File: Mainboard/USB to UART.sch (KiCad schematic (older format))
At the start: 8 parts, among them U9 CH340B

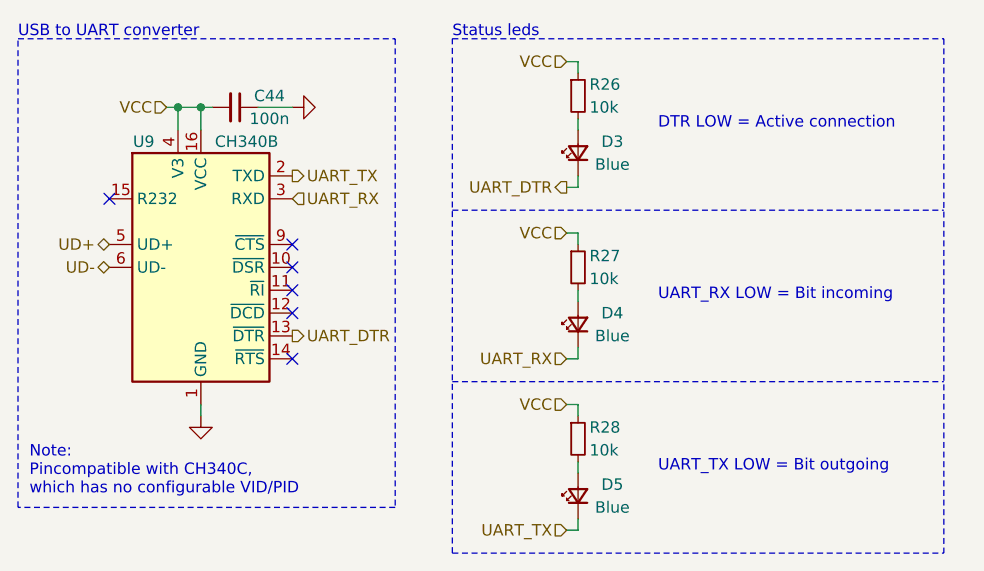
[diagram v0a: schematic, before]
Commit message: Before power tree change
Backup before switching from two to one LDO
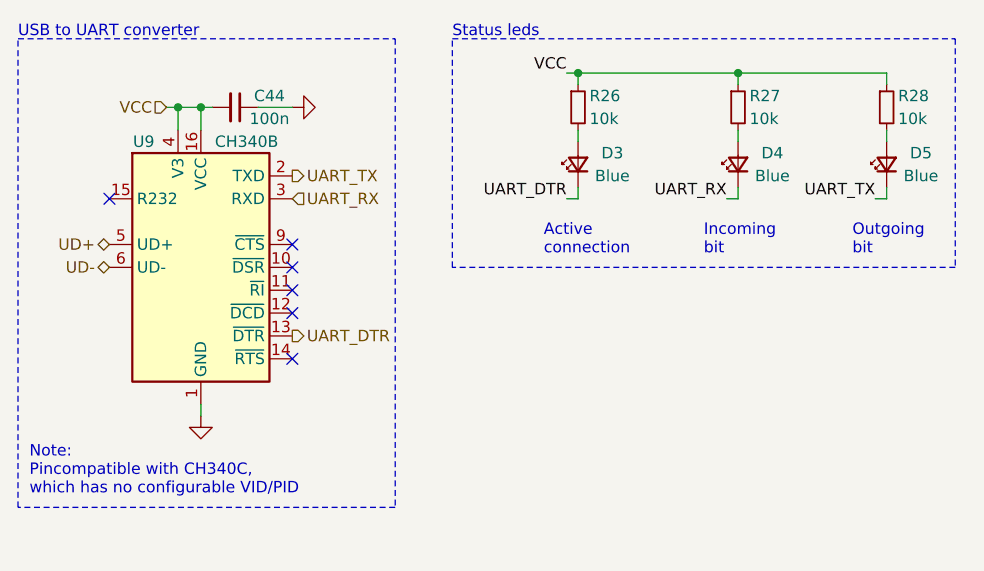
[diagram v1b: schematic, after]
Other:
- note added: "Active\nconnection"
- note added: "Incoming\nbit"
- note added: "Outgoing\nbit"
- note removed: "DTR LOW = Active connection"
- note removed: "UART_RX LOW = Bit incoming"
- note removed: "UART_TX LOW = Bit outgoing"
- moved on the sheet: D3, D4, D5, R26, R27, R28
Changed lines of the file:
@@
 Sheet 2 9
 Title "4x38W amp with DSP and BT"
-Date "2021-06-08"
-Rev "0.1"
+Date "2021-11-08"
+Rev "0.2"
 Comp "ZOUDIO"
 Comment1 ""
@@
 Wire Notes Line
 	5650 2800 5650 4850
-Wire Notes Line
-	5900 5050 8050 5050
-Wire Notes Line
-	5900 4300 8050 4300
-Wire Notes Line
-	5900 3550 8050 3550
 Text Notes 5900 2800 0    50   ~ 0
 Status leds
 Wire Notes Line
-	5900 5050 5900 2800
-Wire Notes Line
-	8050 2800 8050 5050
-Wire Notes Line
-	5900 2800 8050 2800
-Text HLabel 6400 3450 0    50   Output ~ 0
-UART_DTR
-Wire Wire Line
-	6400 4950 6450 4950
-Wire Wire Line
-	6400 4200 6450 4200
-Text HLabel 6400 4950 0    50   Input ~ 0
-UART_TX
-Text HLabel 6400 4200 0    50   Input ~ 0
-UART_RX
-Text Notes 6800 4700 0    50   ~ 0
-UART_TX LOW = Bit outgoing
-Text Notes 6800 3950 0    50   ~ 0
-UART_RX LOW = Bit incoming
-Wire Wire Line
-	6450 3450 6400 3450
-Wire Wire Line
-	6450 3400 6450 3450
-Wire Wire Line
-	6450 2900 6450 2950
-Wire Wire Line
-	6450 3150 6450 3200
+	5900 3800 5900 2800
+Wire Notes Line
+	5900 2800 8100 2800
+Wire Wire Line
+	7750 3500 7800 3500
+Wire Wire Line
+	7100 3500 7150 3500
+Wire Wire Line
+	6450 3500 6400 3500
+Wire Wire Line
+	6450 3450 6450 3500
+Wire Wire Line
+	6450 2950 6450 3000
+Wire Wire Line
+	6450 3200 6450 3250
 $Comp
 L Device:LED_Small D?
 U 1 1 5FD85D21
-P 6450 3300
+P 6450 3350
 AR Path="/5FBDE745/5FD85D21" Ref="D?"  Part="1"
 AR Path="/5FBDE62F/5FD85D21" Ref="D?"  Part="1"
@@
 AR Path="/5FF9E05B/5FD85D21" Ref="D?"  Part="1"
 AR Path="/60A7E145/5FD85D21" Ref="D3"  Part="1"
-F 0 "D3" V 6500 3150 50  0000 C CNN
-F 1 "Blue" V 6400 3150 50  0000 C CNN
-F 2 "LED_SMD:LED_0603_1608Metric" V 6450 3300 50  0001 C CNN
-F 3 "~" V 6450 3300 50  0001 C CNN
-F 4 "Orient" H 6450 3300 50  0001 C CNN "Manufacturer"
-F 5 "ORH-B36G" H 6450 3300 50  0001 C CNN "Partnumber"
-	1    6450 3300
+F 0 "D3" V 6500 3200 50  0000 C CNN
+F 1 "Blue" V 6400 3200 50  0000 C CNN
+F 2 "LED_SMD:LED_0603_1608Metric" V 6450 3350 50  0001 C CNN
+F 3 "~" V 6450 3350 50  0001 C CNN
+F 4 "Orient" H 6450 3350 50  0001 C CNN "Manufacturer"
+F 5 "ORH-B36G" H 6450 3350 50  0001 C CNN "Partnumber"
+	1    6450 3350
 	0    -1   -1   0
 $EndComp
@@
 L Device:R_Small R?
 U 1 1 5FD85D1A
-P 6450 3050
+P 6450 3100
 AR Path="/5FBDE745/5FD85D1A" Ref="R?"  Part="1"
 AR Path="/5FBDE62F/5FD85D1A" Ref="R?"  Part="1"
@@
 AR Path="/5FF9E05B/5FD85D1A" Ref="R?"  Part="1"
 AR Path="/60A7E145/5FD85D1A" Ref="R26"  Part="1"
-F 0 "R26" H 6500 3100 50  0000 L CNN
-F 1 "10k" H 6500 3000 50  0000 L CNN
-F 2 "Resistor_SMD:R_0603_1608Metric" H 6450 3050 50  0001 C CNN
-F 3 "~" H 6450 3050 50  0001 C CNN
-F 4 "Uni-royal" H 6450 3050 50  0001 C CNN "Manufacturer"
-F 5 "0603WAF1002T5E" H 6450 3050 50  0001 C CNN "Partnumber"
-	1    6450 3050
-	1    0    0    -1
-$EndComp
-Wire Wire Line
-	6450 3900 6450 3950
-Wire Wire Line
-	6450 3700 6450 3650
-Wire Wire Line
-	6450 4200 6450 4150
+F 0 "R26" H 6500 3150 50  0000 L CNN
+F 1 "10k" H 6500 3050 50  0000 L CNN
+F 2 "Resistor_SMD:R_0603_1608Metric" H 6450 3100 50  0001 C CNN
+F 3 "~" H 6450 3100 50  0001 C CNN
+F 4 "Uni-royal" H 6450 3100 50  0001 C CNN "Manufacturer"
+F 5 "0603WAF1002T5E" H 6450 3100 50  0001 C CNN "Partnumber"
+	1    6450 3100
+	1    0    0    -1
+$EndComp
+Wire Wire Line
+	7150 3200 7150 3250
+Wire Wire Line
+	7150 3000 7150 2950
+Wire Wire Line
+	7150 3500 7150 3450
 $Comp
 L Device:LED_Small D?
 U 1 1 5FD85D09
-P 6450 4050
+P 7150 3350
 AR Path="/5FBDE62F/5FD85D09" Ref="D?"  Part="1"
 AR Path="/5FD81784/5FD85D09" Ref="D?"  Part="1"
@@
 AR Path="/5FF9E05B/5FD85D09" Ref="D?"  Part="1"
 AR Path="/60A7E145/5FD85D09" Ref="D4"  Part="1"
-F 0 "D4" V 6500 3900 50  0000 C CNN
-F 1 "Blue" V 6400 3900 50  0000 C CNN
-F 2 "LED_SMD:LED_0603_1608Metric" V 6450 4050 50  0001 C CNN
-F 3 "~" V 6450 4050 50  0001 C CNN
-F 4 "Orient" H 6450 4050 50  0001 C CNN "Manufacturer"
-F 5 "ORH-B36G" H 6450 4050 50  0001 C CNN "Partnumber"
-	1    6450 4050
+F 0 "D4" V 7200 3200 50  0000 C CNN
+F 1 "Blue" V 7100 3200 50  0000 C CNN
+F 2 "LED_SMD:LED_0603_1608Metric" V 7150 3350 50  0001 C CNN
+F 3 "~" V 7150 3350 50  0001 C CNN
+F 4 "Orient" H 7150 3350 50  0001 C CNN "Manufacturer"
+F 5 "ORH-B36G" H 7150 3350 50  0001 C CNN "Partnumber"
+	1    7150 3350
 	0    -1   -1   0
 $EndComp
@@
 L Device:R_Small R?
 U 1 1 5FD85D02
-P 6450 3800
+P 7150 3100
 AR Path="/5FBDE745/5FD85D02" Ref="R?"  Part="1"
 AR Path="/5FBDE62F/5FD85D02" Ref="R?"  Part="1"
@@
 AR Path="/5FF9E05B/5FD85D02" Ref="R?"  Part="1"
 AR Path="/60A7E145/5FD85D02" Ref="R27"  Part="1"
-F 0 "R27" H 6500 3850 50  0000 L CNN
-F 1 "10k" H 6500 3750 50  0000 L CNN
-F 2 "Resistor_SMD:R_0603_1608Metric" H 6450 3800 50  0001 C CNN
-F 3 "~" H 6450 3800 50  0001 C CNN
-F 4 "Uni-royal" H 6450 3800 50  0001 C CNN "Manufacturer"
-F 5 "0603WAF1002T5E" H 6450 3800 50  0001 C CNN "Partnumber"
-	1    6450 3800
-	1    0    0    -1
-$EndComp
-Wire Wire Line
-	6450 4650 6450 4700
-Wire Wire Line
-	6450 4450 6450 4400
-Wire Wire Line
-	6450 4950 6450 4900
+F 0 "R27" H 7200 3150 50  0000 L CNN
+F 1 "10k" H 7200 3050 50  0000 L CNN
+F 2 "Resistor_SMD:R_0603_1608Metric" H 7150 3100 50  0001 C CNN
+F 3 "~" H 7150 3100 50  0001 C CNN
+F 4 "Uni-royal" H 7150 3100 50  0001 C CNN "Manufacturer"
+F 5 "0603WAF1002T5E" H 7150 3100 50  0001 C CNN "Partnumber"
+	1    7150 3100
+	1    0    0    -1
+$EndComp
+Wire Wire Line
+	7800 3200 7800 3250
+Wire Wire Line
+	7800 3000 7800 2950
+Wire Wire Line
+	7800 3500 7800 3450
 $Comp
 L Device:LED_Small D?
 U 1 1 5FD85CF1
-P 6450 4800
+P 7800 3350
 AR Path="/5FBDE745/5FD85CF1" Ref="D?"  Part="1"
 AR Path="/5FBDE62F/5FD85CF1" Ref="D?"  Part="1"
@@
 AR Path="/5FF9E05B/5FD85CF1" Ref="D?"  Part="1"
 AR Path="/60A7E145/5FD85CF1" Ref="D5"  Part="1"
-F 0 "D5" V 6500 4650 50  0000 C CNN
-F 1 "Blue" V 6400 4650 50  0000 C CNN
-F 2 "LED_SMD:LED_0603_1608Metric" V 6450 4800 50  0001 C CNN
-F 3 "~" V 6450 4800 50  0001 C CNN
-F 4 "Orient" H 6450 4800 50  0001 C CNN "Manufacturer"
-F 5 "ORH-B36G" H 6450 4800 50  0001 C CNN "Partnumber"
-	1    6450 4800
+F 0 "D5" V 7850 3200 50  0000 C CNN
+F 1 "Blue" V 7750 3200 50  0000 C CNN
+F 2 "LED_SMD:LED_0603_1608Metric" V 7800 3350 50  0001 C CNN
+F 3 "~" V 7800 3350 50  0001 C CNN
+F 4 "Orient" H 7800 3350 50  0001 C CNN "Manufacturer"
+F 5 "ORH-B36G" H 7800 3350 50  0001 C CNN "Partnumber"
+	1    7800 3350
 	0    -1   -1   0
 $EndComp
@@
 L Device:R_Small R?
 U 1 1 5FD85CEA
-P 6450 4550
+P 7800 3100
 AR Path="/5FBDE745/5FD85CEA" Ref="R?"  Part="1"
 AR Path="/5FBDE62F/5FD85CEA" Ref="R?"  Part="1"
@@
 AR Path="/5FF9E05B/5FD85CEA" Ref="R?"  Part="1"
 AR Path="/60A7E145/5FD85CEA" Ref="R28"  Part="1"
-F 0 "R28" H 6500 4600 50  0000 L CNN
-F 1 "10k" H 6500 4500 50  0000 L CNN
-F 2 "Resistor_SMD:R_0603_1608Metric" H 6450 4550 50  0001 C CNN
-F 3 "~" H 6450 4550 50  0001 C CNN
-F 4 "Uni-royal" H 6450 4550 50  0001 C CNN "Manufacturer"
-F 5 "0603WAF1002T5E" H 6450 4550 50  0001 C CNN "Partnumber"
-	1    6450 4550
-	1    0    0    -1
-$EndComp
-Text Notes 6800 3200 0    50   ~ 0
-DTR LOW = Active connection
+F 0 "R28" H 7850 3150 50  0000 L CNN
+F 1 "10k" H 7850 3050 50  0000 L CNN
+F 2 "Resistor_SMD:R_0603_1608Metric" H 7800 3100 50  0001 C CNN
+F 3 "~" H 7800 3100 50  0001 C CNN
+F 4 "Uni-royal" H 7800 3100 50  0001 C CNN "Manufacturer"
+F 5 "0603WAF1002T5E" H 7800 3100 50  0001 C CNN "Partnumber"
+	1    7800 3100
+	1    0    0    -1
+$EndComp
 Wire Wire Line
 	4650 3100 4700 3100
@@
 VCC
 Connection ~ 4700 3100
-Text HLabel 6400 2900 0    50   Input ~ 0
+Wire Wire Line
+	6450 2950 6400 2950
+Text Label 6400 2950 2    50   ~ 0
 VCC
-Wire Wire Line
-	6450 2900 6400 2900
-Text HLabel 6400 3650 0    50   Input ~ 0
-VCC
-Wire Wire Line
-	6400 3650 6450 3650
-Text HLabel 6400 4400 0    50   Input ~ 0
-VCC
-Wire Wire Line
-	6400 4400 6450 4400
+Text Label 6400 3500 2    50   ~ 0
+UART_DTR
+Text Label 7100 3500 2    50   ~ 0
+UART_RX
+Text Label 7750 3500 2    50   ~ 0
+UART_TX
+Wire Wire Line
+	6450 2950 7150 2950
+Connection ~ 6450 2950
+Connection ~ 7150 2950
+Wire Wire Line
+	7150 2950 7800 2950
+Text Notes 6300 3750 0    50   ~ 0
+Active\nconnection
+Text Notes 7000 3750 0    50   ~ 0
+Incoming\nbit
+Text Notes 7650 3750 0    50   ~ 0
+Outgoing\nbit
+Wire Notes Line
+	8100 2800 8100 3800
+Wire Notes Line
+	8100 3800 5900 3800
 $EndSCHEMATC
